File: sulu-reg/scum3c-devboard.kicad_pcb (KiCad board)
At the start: 2 copper layers, 41.7 x 36.1 mm, 55 parts, among them J1 Conn_02x11_Odd_Even, J10 through_hole, J11 through_hole, J12 through_hole, J13 through_hole, J14 through_hole, J15 through_hole, J16 through_hole, J17 through_hole, J18 through_hole, J19 through_hole, J2 Conn_02x10_Odd_Even, J20 through_hole, J21 through_hole, J3 Conn_02x05_Odd_Even, J4 73391-0060, J5 through_hole, J6 through_hole, J7 through_hole, J8 through_hole, J9 through_hole, U1 scum3, U2 S-85S1AB18-I6T1U, U3 S-85S1AB11-I6T1U, U9AB1 ICM-20948

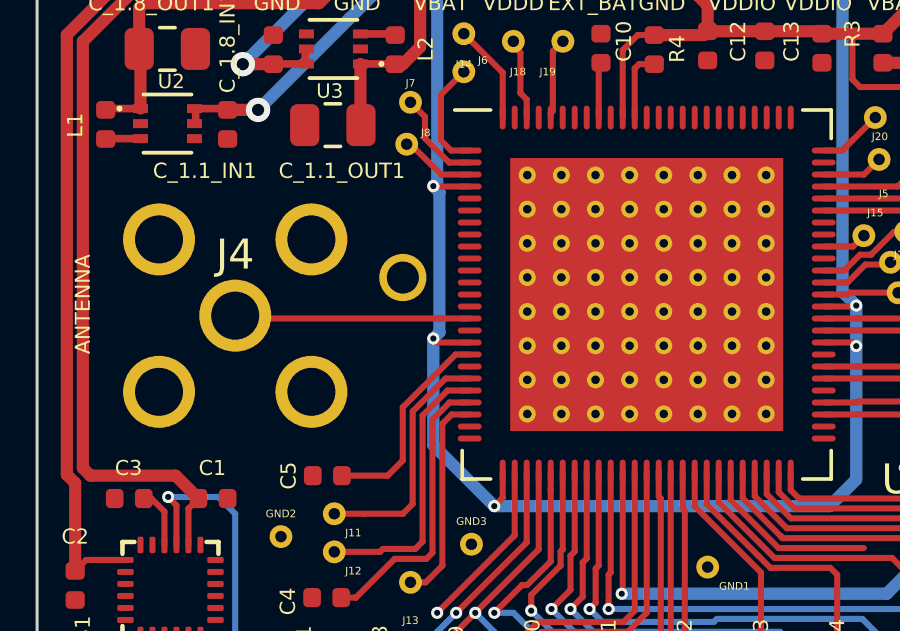
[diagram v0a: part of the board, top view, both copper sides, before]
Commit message: removed vbat under antenna
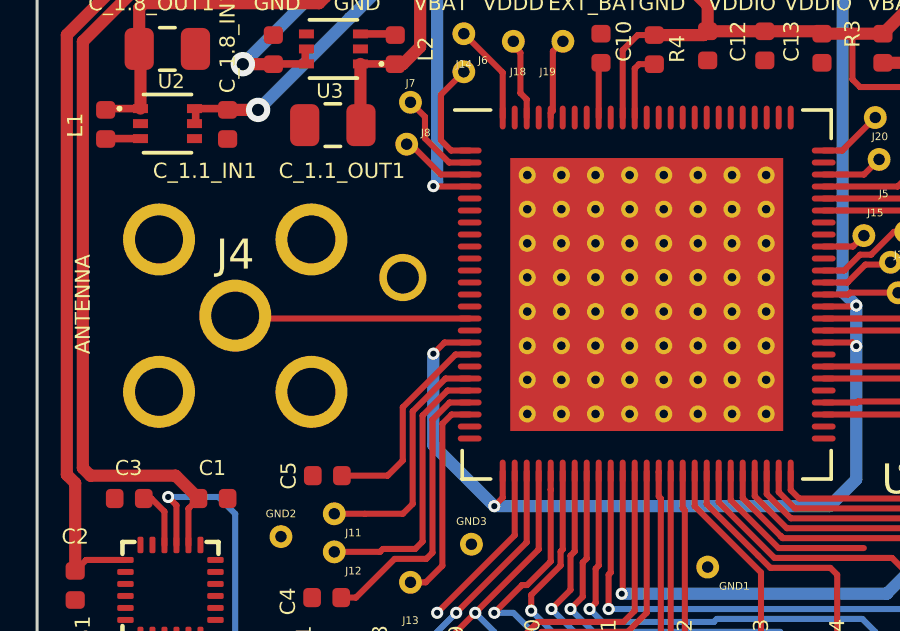
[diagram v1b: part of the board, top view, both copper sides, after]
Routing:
- net +VBAT: track 88.1 -> 82.4 mm

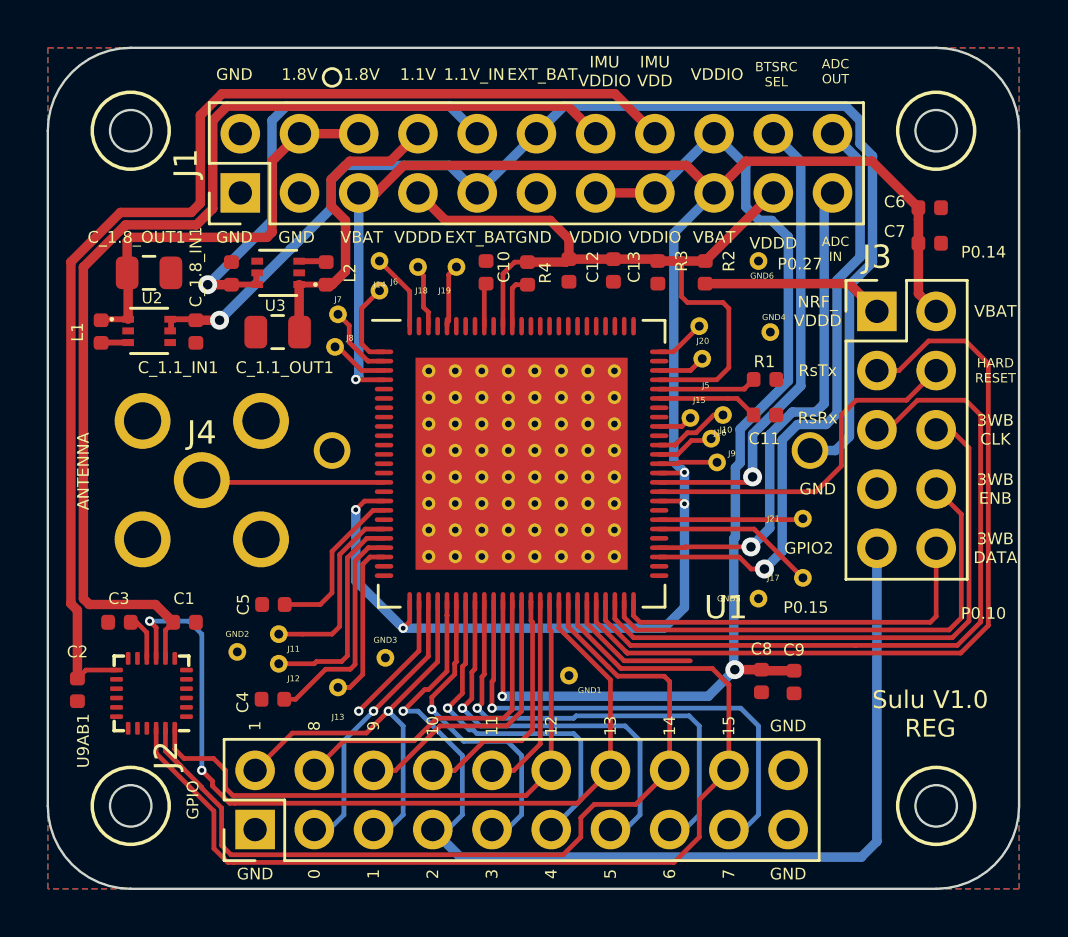
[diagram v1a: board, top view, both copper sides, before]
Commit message: moved battery north a little
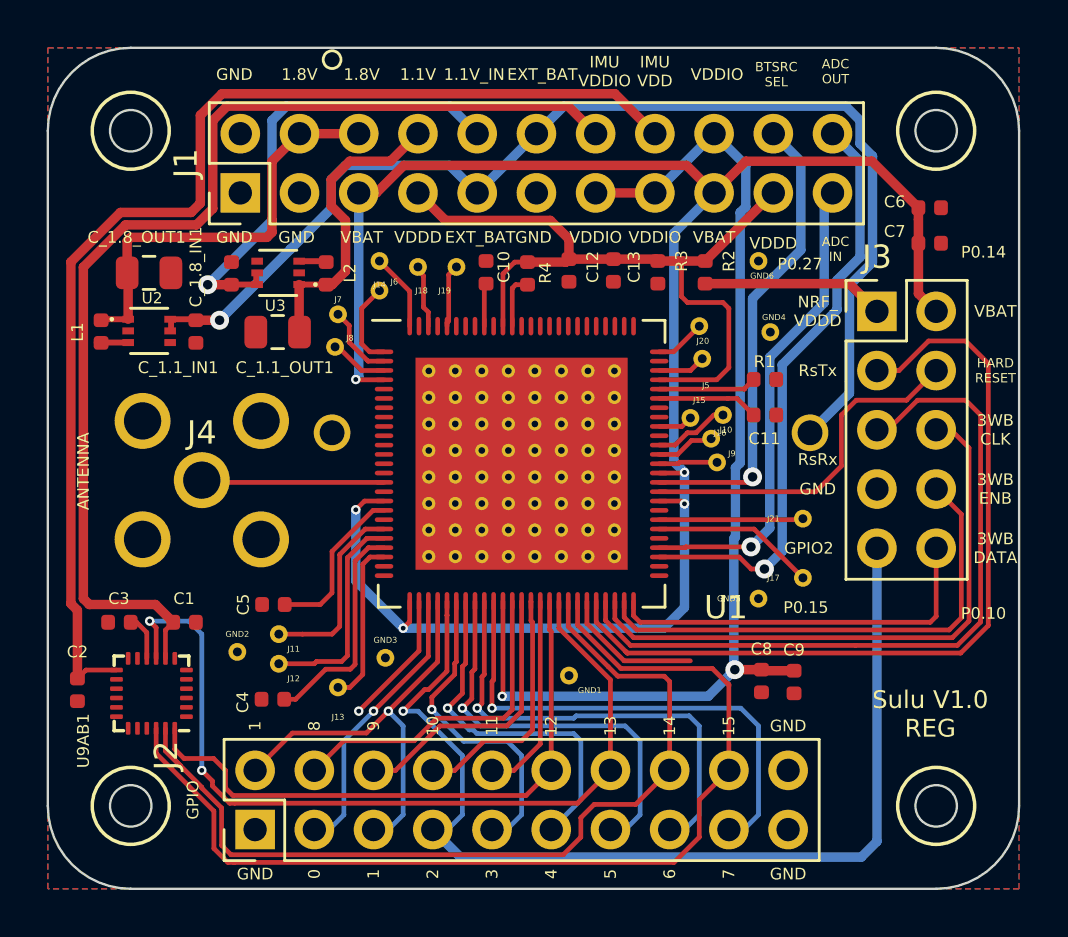
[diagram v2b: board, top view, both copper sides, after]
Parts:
- moved B1 0.76 mm to (124.7, 89.0)
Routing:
- net +VDDIO: track 48.8 -> 47.0 mm
- net +EXT_BAT: track 51.8 -> 50.4 mm
- net /SENSOR_LDO_OUTPUT: track 26.3 -> 25.6 mm
- net /SENSOR_EXT_IN: track 21.2 -> 20.6 mm
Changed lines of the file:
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@@
     (thickness 1.6)
     (drawings 783)
-    (tracks 516)
+    (tracks 508)
     (zones 0)
     (modules 55)
@@
   )
   (setup
-    (last_trace_width 0.2032)
+    (last_trace_width 0.4064)
     (user_trace_width 0.127)
     (user_trace_width 0.2032)
@@
   )
   (module downloaded_libs:BH1000G (layer B.Cu)
-    (at 124.7394 89.789 270)
+    (at 124.7394 89.027 270)
     (fp_text reference B1 (at 0 -3.7465 270) (layer B.SilkS)
       (effects (font (size 1 1) (thickness 0.15)) (justify mirror))
@@
     (effects (font (size 0.5 0.5) (thickness 0.1)) (justify mirror))
   )
-  (gr_text RsRx (at 139.065 88.392) (layer B.SilkS)
+  (gr_text RsRx (at 139.065 90.17) (layer B.SilkS)
     (effects (font (size 0.5 0.5) (thickness 0.1)) (justify mirror))
   )
@@
     (effects (font (size 0.5 0.5) (thickness 0.1)))
   )
-  (gr_text RsRx (at 139.065 88.392) (layer F.SilkS)
+  (gr_text RsRx (at 139.065 90.17) (layer F.SilkS)
     (effects (font (size 0.5 0.5) (thickness 0.1)))
   )
@@
   (segment (start 134.366 100.33) (end 135.509 99.187) (width 0.4064) (layer B.Cu) (net 4))
   (segment (start 125.5332 100.33) (end 134.366 100.33) (width 0.4064) (layer B.Cu) (net 4))
-  (segment (start 135.466386 99.144386) (end 135.509 99.187) (width 0.4064) (layer B.Cu) (net 4))
-  (segment (start 135.466386 93.567444) (end 135.466386 99.144386) (width 0.4064) (layer B.Cu) (net 4))
-  (segment (start 135.73758 90.32242) (end 135.534389 90.525611) (width 0.4064) (layer B.Cu) (net 4))
-  (segment (start 135.534389 90.525611) (end 135.534389 93.499441) (width 0.4064) (layer B.Cu) (net 4))
-  (segment (start 136.562201 79.920201) (end 137.093783 79.920201) (width 0.4064) (layer B.Cu) (net 4))
-  (segment (start 135.979799 79.337799) (end 136.562201 79.920201) (width 0.4064) (layer B.Cu) (net 4))
-  (segment (start 135.534389 93.499441) (end 135.466386 93.567444) (width 0.4064) (layer B.Cu) (net 4))
-  (segment (start 135.979799 77.559799) (end 135.979799 79.337799) (width 0.4064) (layer B.Cu) (net 4))
-  (segment (start 137.806791 80.633209) (end 137.806791 86.799894) (width 0.4064) (layer B.Cu) (net 4))
-  (segment (start 134.62 76.2) (end 135.979799 77.559799) (width 0.4064) (layer B.Cu) (net 4))
-  (segment (start 137.806791 86.799894) (end 135.73758 88.869105) (width 0.4064) (layer B.Cu) (net 4))
-  (segment (start 137.093783 79.920201) (end 137.806791 80.633209) (width 0.4064) (layer B.Cu) (net 4))
-  (segment (start 135.73758 88.869105) (end 135.73758 90.32242) (width 0.4064) (layer B.Cu) (net 4))
+  (segment (start 135.979799 77.559799) (end 134.62 76.2) (width 0.4064) (layer B.Cu) (net 4))
+  (segment (start 135.979799 79.337799) (end 135.979799 77.559799) (width 0.4064) (layer B.Cu) (net 4))
+  (segment (start 135.73758 79.580018) (end 135.979799 79.337799) (width 0.4064) (layer B.Cu) (net 4))
+  (segment (start 135.73758 90.32242) (end 135.73758 79.580018) (width 0.4064) (layer B.Cu) (net 4))
+  (segment (start 135.509 99.187) (end 135.466386 99.144386) (width 0.4064) (layer B.Cu) (net 4))
+  (segment (start 135.534389 93.499441) (end 135.534389 90.525611) (width 0.4064) (layer B.Cu) (net 4))
+  (segment (start 135.466386 99.144386) (end 135.466386 93.567444) (width 0.4064) (layer B.Cu) (net 4))
+  (segment (start 135.466386 93.567444) (end 135.534389 93.499441) (width 0.4064) (layer B.Cu) (net 4))
+  (segment (start 135.534389 90.525611) (end 135.73758 90.32242) (width 0.4064) (layer B.Cu) (net 4))
   (segment (start 135.607 87.555) (end 136.317 88.265) (width 0.2032) (layer F.Cu) (net 5))
   (segment (start 135.203 87.555) (end 135.607 87.555) (width 0.2032) (layer F.Cu) (net 5))
@@
   (via (at 136.779 94.869) (size 0.8128) (drill 0.4064) (layers F.Cu B.Cu) (net 20))
   (segment (start 135.697172 94.355) (end 136.211172 94.869) (width 0.2032) (layer F.Cu) (net 20))
-  (segment (start 140.880201 81.496083) (end 139.891389 82.484894) (width 0.4064) (layer B.Cu) (net 20))
-  (segment (start 139.7 76.2) (end 140.880201 77.380201) (width 0.4064) (layer B.Cu) (net 20))
-  (segment (start 140.880201 77.380201) (end 140.880201 81.496083) (width 0.4064) (layer B.Cu) (net 20))
-  (segment (start 139.891389 82.484894) (end 139.891389 88.200611) (width 0.4064) (layer B.Cu) (net 20))
-  (segment (start 138.198351 88.671399) (end 137.541 89.32875) (width 0.4064) (layer B.Cu) (net 20))
-  (segment (start 139.891389 88.200611) (end 139.420601 88.671399) (width 0.4064) (layer B.Cu) (net 20))
-  (segment (start 139.420601 88.671399) (end 138.198351 88.671399) (width 0.4064) (layer B.Cu) (net 20))
-  (segment (start 137.541 94.107) (end 136.779 94.869) (width 0.4064) (layer B.Cu) (net 20))
-  (segment (start 137.541 89.32875) (end 137.541 94.107) (width 0.4064) (layer B.Cu) (net 20))
+  (segment (start 140.880201 77.380201) (end 139.7 76.2) (width 0.4064) (layer B.Cu) (net 20))
+  (segment (start 140.880201 81.496083) (end 140.880201 77.380201) (width 0.4064) (layer B.Cu) (net 20))
+  (segment (start 136.779 94.869) (end 137.541 94.107) (width 0.4064) (layer B.Cu) (net 20))
+  (segment (start 137.541 86.107778) (end 139.891389 83.757389) (width 0.4064) (layer B.Cu) (net 20))
+  (segment (start 139.891389 83.757389) (end 139.891389 82.484894) (width 0.4064) (layer B.Cu) (net 20))
+  (segment (start 137.541 94.107) (end 137.541 86.107778) (width 0.4064) (layer B.Cu) (net 20))
+  (segment (start 139.891389 82.484894) (end 140.880201 81.496083) (width 0.4064) (layer B.Cu) (net 20))
   (via (at 136.202987 93.921013) (size 0.8128) (drill 0.4064) (layers F.Cu B.Cu) (net 21))
   (segment (start 132.265 93.955) (end 133.375 93.955) (width 0.2032) (layer F.Cu) (net 21))
@@
   (segment (start 133.375 93.955) (end 133.408987 93.921013) (width 0.2032) (layer F.Cu) (net 21))
   (segment (start 139.342312 79.097688) (end 139.7 78.74) (width 0.4064) (layer B.Cu) (net 21))
-  (segment (start 139.342312 87.780312) (end 139.342312 79.097688) (width 0.4064) (layer B.Cu) (net 21))
+  (segment (start 137.00759 85.786988) (end 139.342312 83.452266) (width 0.4064) (layer B.Cu) (net 21))
+  (segment (start 139.342312 83.452266) (end 139.342312 79.097688) (width 0.4064) (layer B.Cu) (net 21))
+  (segment (start 137.00759 93.11641) (end 137.00759 85.786988) (width 0.4064) (layer B.Cu) (net 21))
   (segment (start 136.202987 93.921013) (end 137.00759 93.11641) (width 0.4064) (layer B.Cu) (net 21))
-  (segment (start 137.977406 88.137989) (end 138.984635 88.137989) (width 0.4064) (layer B.Cu) (net 21))
-  (segment (start 137.00759 93.11641) (end 137.00759 89.107806) (width 0.4064) (layer B.Cu) (net 21))
-  (segment (start 137.00759 89.107806) (end 137.977406 88.137989) (width 0.4064) (layer B.Cu) (net 21))
-  (segment (start 138.984635 88.137989) (end 139.342312 87.780312) (width 0.4064) (layer B.Cu) (net 21))
   (segment (start 126.365 102.235) (end 124.76867 102.235) (width 0.2032) (layer F.Cu) (net 22))
   (segment (start 124.76867 102.235) (end 123.49867 103.505) (width 0.2032) (layer F.Cu) (net 22))
@@
   (segment (start 125.593224 101.26979) (end 125.965 100.898014) (width 0.2032) (layer F.Cu) (net 24))
   (segment (start 135.667 91.155) (end 132.265 91.155) (width 0.2032) (layer F.Cu) (net 25))
-  (segment (start 138.340201 77.380201) (end 138.340201 87.020839) (width 0.4064) (layer B.Cu) (net 25))
-  (segment (start 137.16 76.2) (end 138.340201 77.380201) (width 0.4064) (layer B.Cu) (net 25))
   (via (at 136.27099 90.92) (size 0.8128) (drill 0.4064) (layers F.Cu B.Cu) (net 25))
-  (segment (start 138.340201 87.020839) (end 136.27099 89.09005) (width 0.4064) (layer B.Cu) (net 25))
-  (segment (start 136.27099 89.09005) (end 136.27099 90.92) (width 0.4064) (layer B.Cu) (net 25))
   (segment (start 136.03599 91.155) (end 136.27099 90.92) (width 0.2032) (layer F.Cu) (net 25))
   (segment (start 135.667 91.155) (end 136.03599 91.155) (width 0.2032) (layer F.Cu) (net 25))
+  (segment (start 138.340201 77.380201) (end 137.16 76.2) (width 0.4064) (layer B.Cu) (net 25))
+  (segment (start 136.27099 83.259412) (end 138.340201 81.190201) (width 0.4064) (layer B.Cu) (net 25))
+  (segment (start 138.340201 81.190201) (end 138.340201 77.380201) (width 0.4064) (layer B.Cu) (net 25))
+  (segment (start 136.27099 90.92) (end 136.27099 83.259412) (width 0.4064) (layer B.Cu) (net 25))
   (segment (start 130.175 99.620895) (end 130.175 103.505) (width 0.2032) (layer F.Cu) (net 26) (status 20))
   (segment (start 127.965 96.255) (end 127.965 97.410895) (width 0.2032) (layer F.Cu) (net 26) (status 10))
@@
   (segment (start 112.395 84.201) (end 113.411 84.201) (width 0.4064) (layer F.Cu) (net 56) (status 10))
   (segment (start 113.411 84.201) (end 116.466646 81.145354) (width 0.4064) (layer B.Cu) (net 56))
-  (segment (start 139.827 89.789) (end 138.7348 89.789) (width 0.4064) (layer B.Cu) (net 56))
-  (segment (start 140.424799 89.191201) (end 139.827 89.789) (width 0.4064) (layer B.Cu) (net 56))
-  (segment (start 140.424799 82.705841) (end 140.424799 89.191201) (width 0.4064) (layer B.Cu) (net 56))
   (segment (start 141.413611 81.717029) (end 140.424799 82.705841) (width 0.4064) (layer B.Cu) (net 56))
   (segment (start 141.413611 77.159256) (end 141.413611 81.717029) (width 0.4064) (layer B.Cu) (net 56))
@@
   (segment (start 140.266497 75.019799) (end 140.880201 75.633503) (width 0.4064) (layer B.Cu) (net 56))
   (segment (start 127 76.2) (end 128.180201 75.019799) (width 0.4064) (layer B.Cu) (net 56))
+  (segment (start 140.424799 87.337001) (end 140.424799 86.830799) (width 0.4064) (layer B.Cu) (net 56))
+  (segment (start 140.424799 82.705841) (end 140.424799 86.830799) (width 0.4064) (layer B.Cu) (net 56))
+  (segment (start 138.7348 89.027) (end 140.424799 87.337001) (width 0.4064) (layer B.Cu) (net 56))
   (segment (start 116.862999 82.669) (end 116.862999 84.940001) (width 0.2032) (layer F.Cu) (net 57) (status 30))
   (segment (start 116.822999 82.669) (end 118.021 82.669) (width 0.254) (layer F.Cu) (net 57) (status 30))

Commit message: changed front ground to exclude antenna region
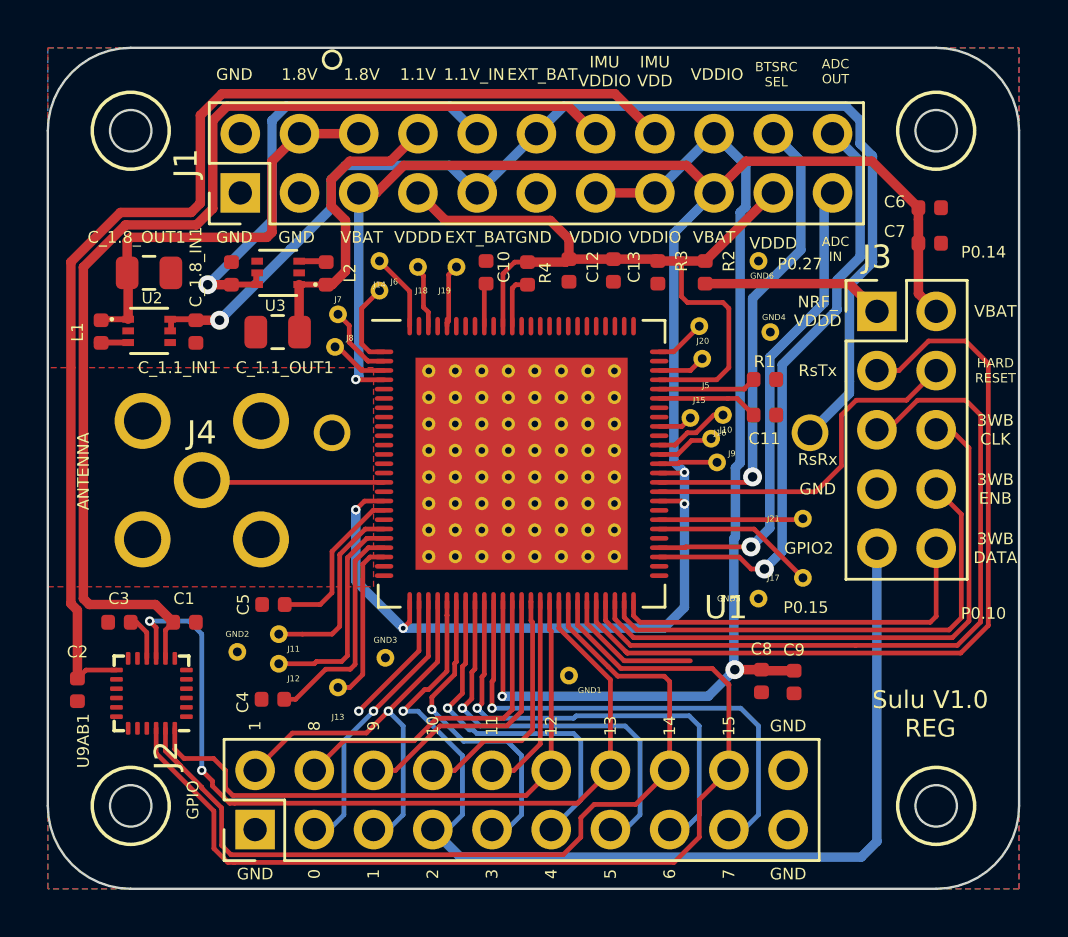
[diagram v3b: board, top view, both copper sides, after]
